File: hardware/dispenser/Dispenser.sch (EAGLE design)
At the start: 64 parts, among them J1 AVR_Prog, J2 RJ45-8PTH, Q1 NFET-SO8, Q2 NFET, Q3 NFET, Q4 NFET, Q5 MOSFET-NCHANNELSMD, U1 ATMEGA168, U10 HALL-EFFECT, U2 OPAMP-DUAL, U3 OPTO-TLP185, U4 MPX10DP, U5 VREG-5V-LDO-AP1117SOT89-3L, U6 WS2801, U7 HALL-EFFECT, U8 HALL-EFFECT, U9 HALL-EFFECT

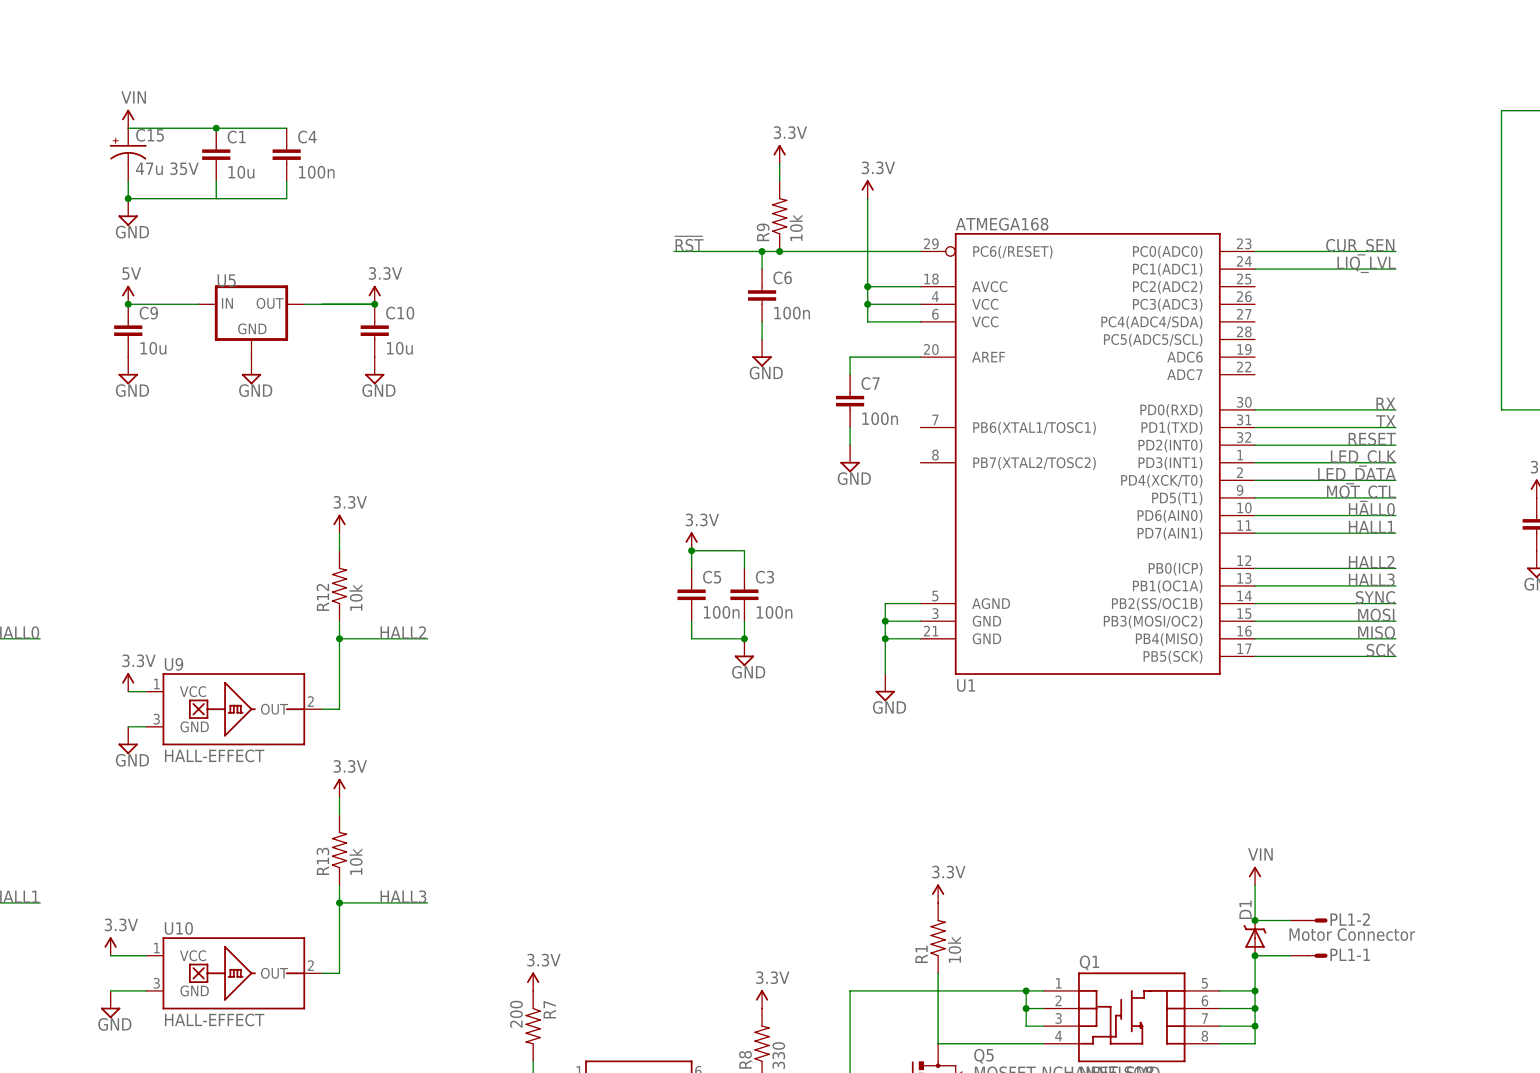
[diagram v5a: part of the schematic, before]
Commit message: Finished Dispenser Layout!
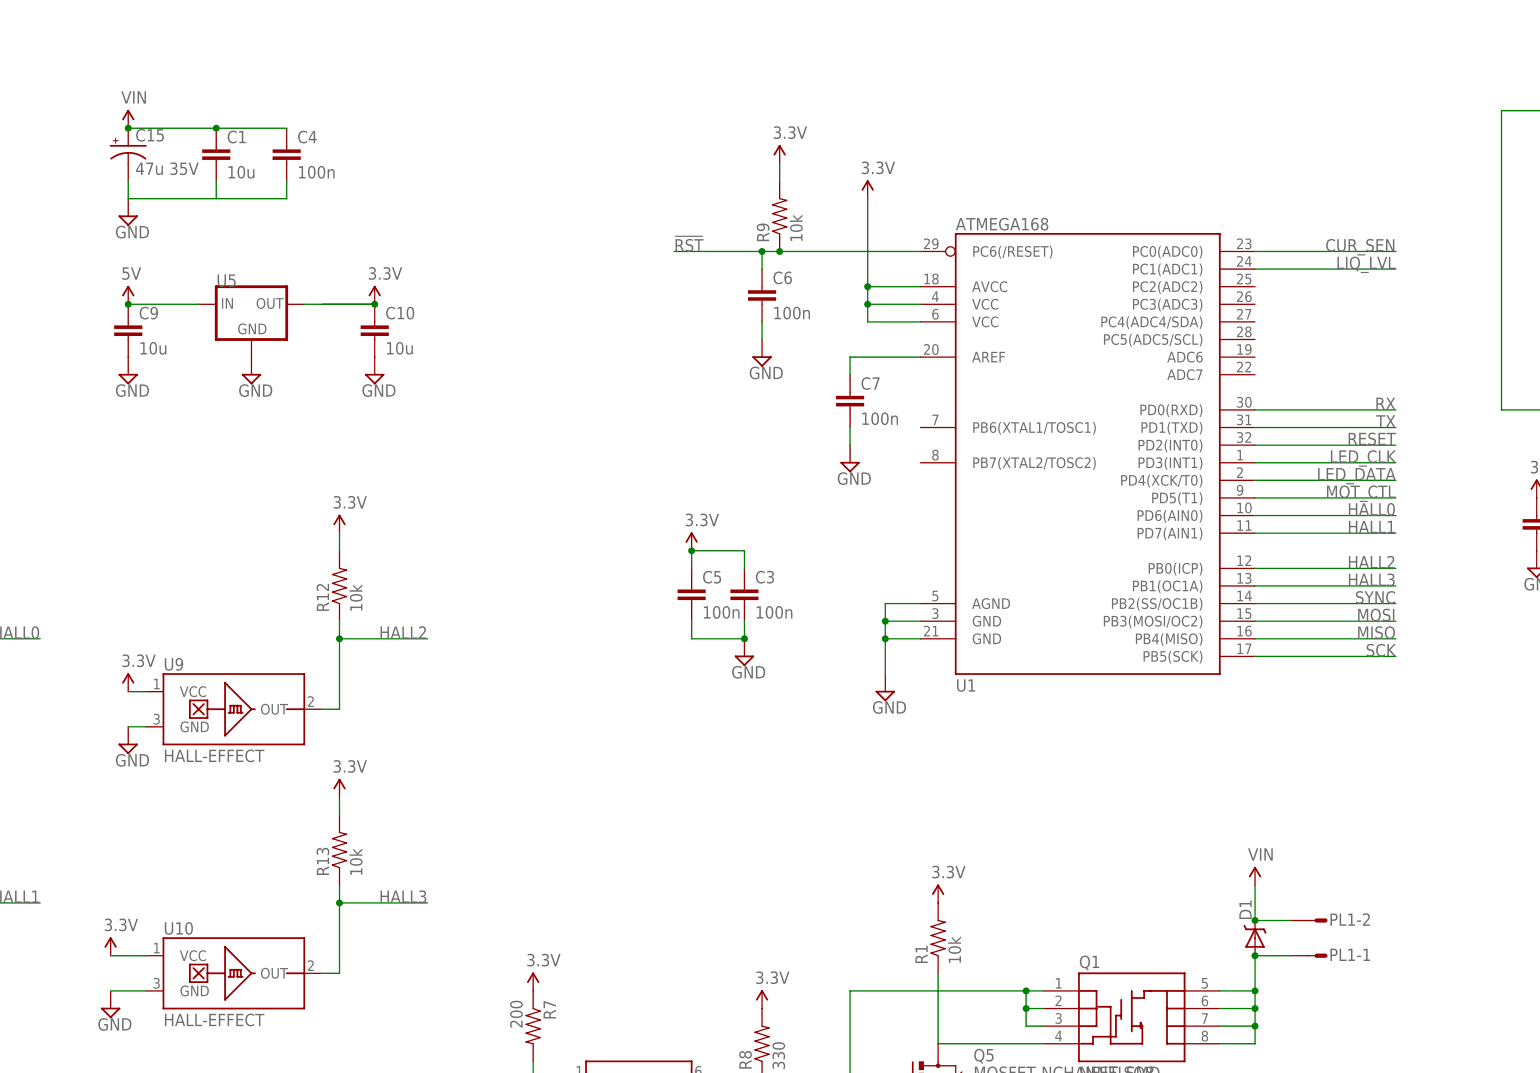
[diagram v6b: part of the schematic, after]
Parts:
- PL1: value Motor Connector -> (none)
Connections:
- removed net N$15: C15.-
- net GND: now also C15.-
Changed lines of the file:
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@@
 <part name="Q3" library="SparkFun-DiscreteSemi" deviceset="MOSFET-NCHANNEL" device="SMD" value="NFET"/>
 <part name="Q4" library="SparkFun-DiscreteSemi" deviceset="MOSFET-NCHANNEL" device="SMD" value="NFET"/>
-<part name="PL1" library="con-hirose-df3" deviceset="DF3-02" device="P" value="Motor Connector"/>
+<part name="PL1" library="con-hirose-df3" deviceset="DF3-02" device="P"/>
 <part name="U5" library="pierre" deviceset="VREG-5V-LDO-AP1117" device="SOT89-3L"/>
 <part name="C9" library="SparkFun-Passives" deviceset="CAP" device="0603-CAP" value="10u"/>
@@
 <wire x1="106.68" y1="218.44" x2="106.68" y2="215.9" width="0.1524" layer="91"/>
 <wire x1="106.68" y1="215.9" x2="96.52" y2="215.9" width="0.1524" layer="91"/>
-<junction x="83.82" y="215.9"/>
 <wire x1="83.82" y1="215.9" x2="96.52" y2="215.9" width="0.1524" layer="91"/>
 <wire x1="96.52" y1="215.9" x2="96.52" y2="218.44" width="0.1524" layer="91"/>
+<pinref part="C15" gate="G$1" pin="-"/>
+<wire x1="83.82" y1="218.44" x2="83.82" y2="215.9" width="0.1524" layer="91"/>
 </segment>
 <segment>
@@
 <pinref part="C15" gate="G$1" pin="+"/>
 <wire x1="96.52" y1="226.06" x2="83.82" y2="226.06" width="0.1524" layer="91"/>
+<junction x="83.82" y="226.06"/>
 </segment>
 <segment>
@@
 </segment>
 </net>
-<net name="N$15" class="0">
-<segment>
-<pinref part="C15" gate="G$1" pin="-"/>
-<wire x1="83.82" y1="218.44" x2="83.82" y2="215.9" width="0.1524" layer="91"/>
-</segment>
-</net>

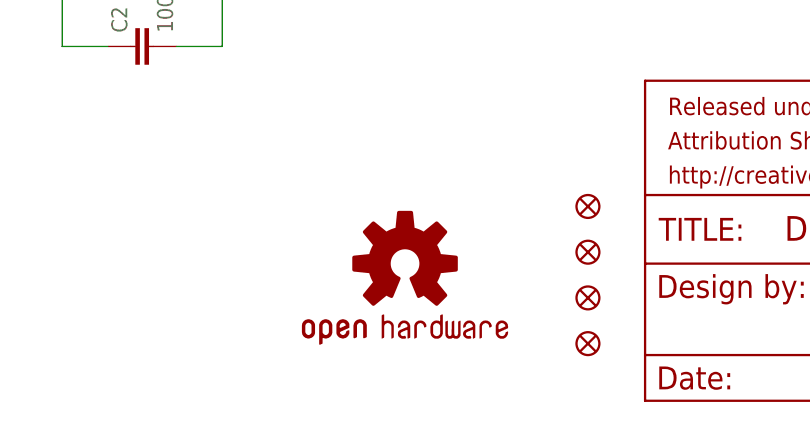
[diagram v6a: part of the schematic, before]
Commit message: cleaned up dispenser layout silkscreen and design rules.
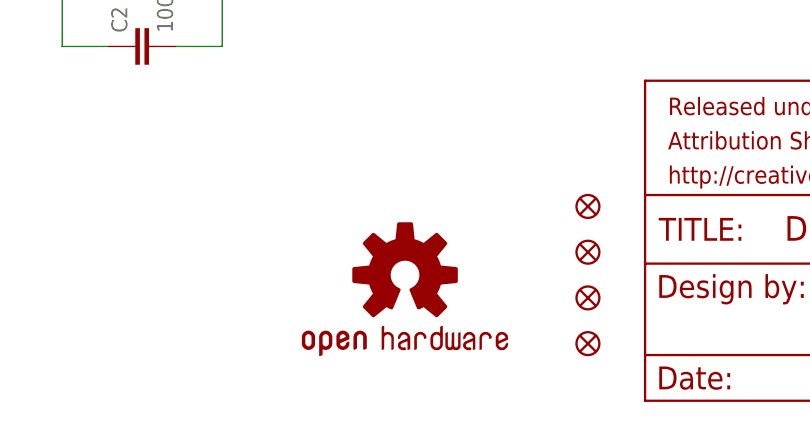
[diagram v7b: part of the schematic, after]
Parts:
- removed U$4: OSHW-LOGOS, SparkFun-Aesthetics:OSHW-LOGOS
- added U$1: OSHW-LOGOM, pierre:OSHW-LOGOM
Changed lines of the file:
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@@
 <layer number="19" name="Unrouted" color="6" fill="1" visible="no" active="no"/>
 <layer number="20" name="Dimension" color="15" fill="1" visible="no" active="no"/>
-<layer number="21" name="tPlace" color="7" fill="1" visible="no" active="no"/>
-<layer number="22" name="bPlace" color="7" fill="1" visible="no" active="no"/>
+<layer number="21" name="tPlace" color="16" fill="1" visible="no" active="no"/>
+<layer number="22" name="bPlace" color="14" fill="1" visible="no" active="no"/>
 <layer number="23" name="tOrigins" color="15" fill="1" visible="no" active="no"/>
 <layer number="24" name="bOrigins" color="15" fill="1" visible="no" active="no"/>
@@
 <layer number="49" name="Reference" color="7" fill="1" visible="no" active="no"/>
 <layer number="50" name="dxf" color="7" fill="1" visible="no" active="no"/>
-<layer number="51" name="tDocu" color="7" fill="1" visible="no" active="no"/>
+<layer number="51" name="tDocu" color="6" fill="1" visible="no" active="no"/>
 <layer number="52" name="bDocu" color="7" fill="1" visible="no" active="no"/>
 <layer number="53" name="tGND_GNDA" color="7" fill="9" visible="no" active="no"/>
@@
 <part name="LED3" library="pierre" deviceset="RGBLED" device="5050"/>
 <part name="LED4" library="pierre" deviceset="RGBLED" device="5050"/>
-<part name="U$4" library="SparkFun-Aesthetics" deviceset="OSHW-LOGO" device="S"/>
 <part name="FRAME3" library="SparkFun-Aesthetics" deviceset="FRAME-LETTER" device=""/>
 <part name="JP5" library="SparkFun-Aesthetics" deviceset="FIDUCIAL" device="1X2"/>
@@
 <part name="C12" library="SparkFun-Capacitors" deviceset="CAP_POL" device="D" value="100u 6.3V"/>
 <part name="C15" library="SparkFun-Capacitors" deviceset="CAP_POL" device="D" value="47u 35V"/>
+<part name="U$1" library="pierre" deviceset="OSHW-LOGO" device="M"/>
 </parts>
 <sheets>
@@
 <instance part="LED3" gate="G$1" x="353.06" y="190.5" rot="MR270"/>
 <instance part="LED4" gate="G$1" x="353.06" y="177.8" rot="MR270"/>
-<instance part="U$4" gate="G$1" x="256.54" y="19.05"/>
 <instance part="FRAME3" gate="G$2" x="283.21" y="3.81"/>
 <instance part="JP5" gate="G$1" x="276.86" y="20.32"/>
@@
 <instance part="C12" gate="G$1" x="259.08" y="60.96"/>
 <instance part="C15" gate="G$1" x="83.82" y="223.52"/>
+<instance part="U$1" gate="G$1" x="256.54" y="17.78"/>
 </instances>
 <busses>

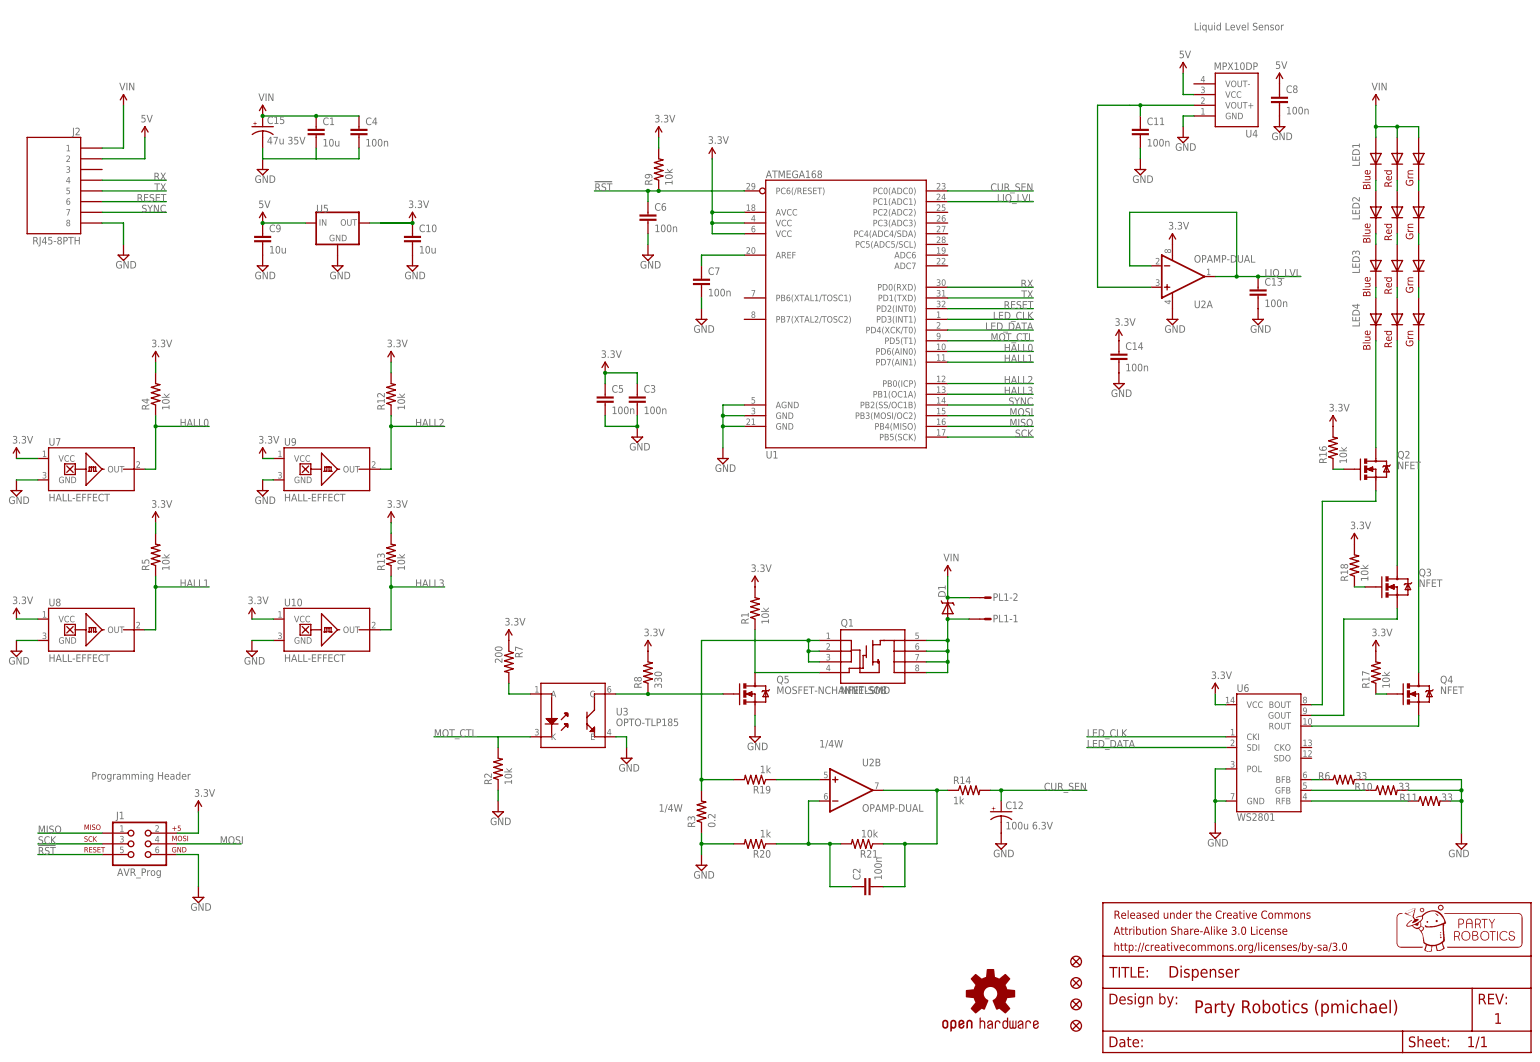
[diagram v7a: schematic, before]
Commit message: Checking in the final dispenser schematics for the kickstarter dispensers
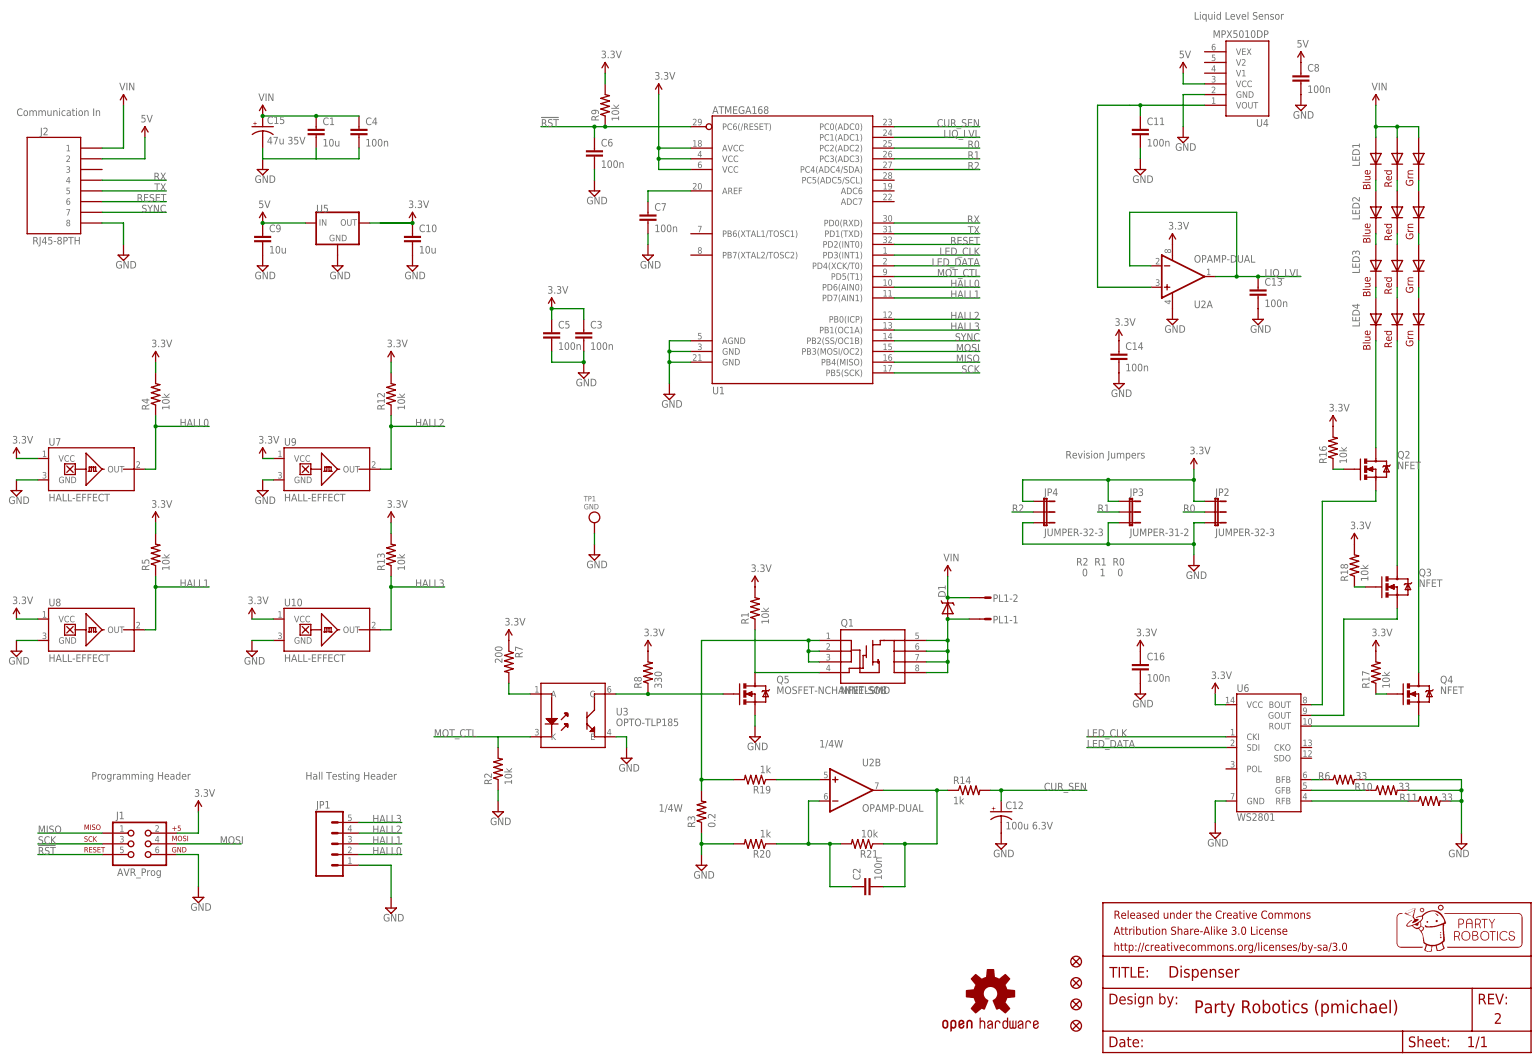
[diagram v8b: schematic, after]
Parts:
- added C16: 100n, SparkFun:CAP0603-CAP
- added JP1: (no value), SparkFun:M051.27MM
- added JP2, JP4: JUMPER-32-3, SparkFun-Passives:JUMPER-32-3
- added JP3: JUMPER-31-2, SparkFun-Passives:JUMPER-31-2
- added TP1: GND, microbuilder:TESTPOINT
- J2: device SparkFun:RJ45-8PTH -> pierre:RJ45-8PTH
- PL1: device con-hirose-df3:DF3-02P -> pierre:DF3-02P
- U4: value MPX10DP -> MPX5010DP; device pierre:MPX10DP -> pierre:MPX5010DP
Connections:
- new net R0: JP2.2, U1.PC2(ADC2)
- new net R1: JP3.2, U1.PC3(ADC3)
- new net R2: JP4.2, U1.PC4(ADC4/SDA)
- net 3.3V: now also C16.1, JP2.1, JP3.1, JP4.1
- net GND: now also C16.2, JP1.1, JP2.3, JP3.3, JP4.3, TP1.P$1; no longer U6.POL
- net HALL0: now also JP1.2
- net HALL1: now also JP1.3
- net HALL2: now also JP1.4
- net HALL3: now also JP1.5
- net N$26: now also U4.VOUT; no longer U4.VOUT+
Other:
- note added: "0 1 0"
- note added: "2"
- note added: "Communication In"
- note added: "Hall Testing Header"
- note added: "R2 R1 R0"
- note added: "Revision Jumpers"
- note removed: "1"
- moved on the sheet: C3, C5, C6, C7, C8, PL1-1, PL1-2, R9, U1
